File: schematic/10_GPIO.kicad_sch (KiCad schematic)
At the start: 2 parts, among them J12 GPIO_P0.00-15, J13 GPIO_P0.16-31

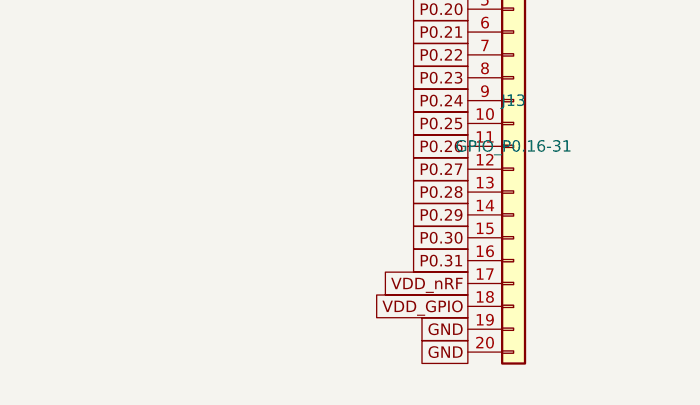
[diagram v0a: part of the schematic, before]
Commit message: Schematic: GNSS COEX0 bias switch, 3.3V VDD_GPIO, DNP RF shunts
- Add U3 TPS22919DCKR on 04_GNSS (COEX0-gated bias); FB5 0402
- Swap U2 to TLV73333 (3.3 V VDD_GPIO); DNP Class-C shunt caps
- Quarantine leftover schematics/; remove stale ERC rpt
- Add PM/DFM/RF/schematic/layout review docs under docs/
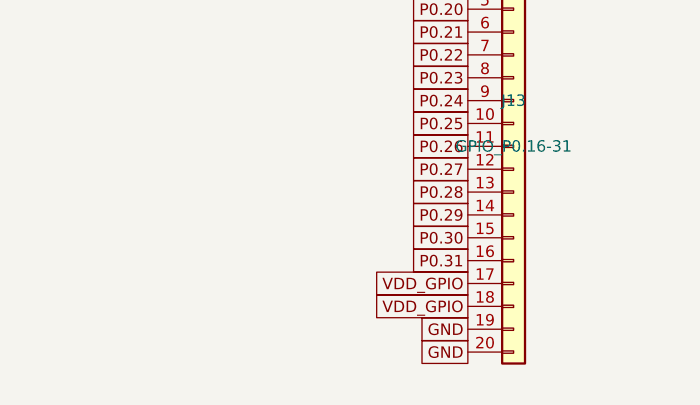
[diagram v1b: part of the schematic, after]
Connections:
- net VDD_nRF is gone; now on net VDD_GPIO: J13.17 (Pin_17)
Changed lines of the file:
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@@
 		)
 	)
-	(global_label "VDD_nRF"
+	(global_label "VDD_GPIO"
 		(at 134.61999999999998 68.58 180)
 		(effects
